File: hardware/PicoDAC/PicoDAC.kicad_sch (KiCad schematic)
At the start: 0 parts

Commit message: added level shifters, finished DAC schematics
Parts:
- added C1, C15, C16, C2, C3: 0.1uF, symbol Device:C_Small
- added C10, C11, C12, C13, C14, C5, C6, C9: 2.2uF, symbol Device:C_Small
- added C4: 4.7uF, symbol Device:C_Small
- added C7, C8: 15uF, symbol Device:C_Small
- added CN1: PJ-327A 5JJ, easyeda2kicad:AUDIO-SMD_PJ-327A5JJ, symbol easyeda2kicad:PJ-327A5JJ
- added R1, R2, R3: 10k, symbol Device:R_Small
- added R4: 200k, symbol Device:R_Small
- added R5, R6, R7, R8: 4.7k, symbol Device:R_Small
- added U1: CS43131-CNZR, easyeda2kicad:TQFN-40_L5.0-W5.0-P0.40-TL-EP3.5, symbol easyeda2kicad:CS43131-CNZR
- added U2: XIAO-RP2350-DIP, Seeed Studio XIAO Series Library:XIAO-RP2350-DIP, symbol Seeed_Studio_XIAO_Series:XIAO-RP2350-DIP
- added U3: PCA9306DCUR, easyeda2kicad:SSOP-8_L2.0-W2.3-P0.50-LS3.1-BR, symbol easyeda2kicad:PCA9306DCUR
- added U4: SN74AXC4T245PWR, easyeda2kicad:TSSOP-16_L5.0-W4.4-P0.65-LS6.4-BL, symbol easyeda2kicad:SN74AXC4T245PWR
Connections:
- new net: R6.2, U3.6 (SCL2)
- new net: R5.1, U3.5 (SDA2)
- new net: R4.2, U3.7 (VREF2), U3.8 (EN)
- new net: C8.2, C9.2, U1.9 (-VA)
- new net: C11.1, U1.21 (VCP_FILT+)
- new net: C14.1, U1.11 (FLYN_VA)
- new net: C14.2, U1.10 (FLYP_VA)
- new net: C12.2, U1.18 (VCP_FILT–)
- new net: C13.2, U1.20 (FLYN_VCP)
- new net: C13.1, C5.1, U1.23 (FLYC_VCP)
- new net: C5.2, U1.24 (FLYP_VCP)
- new net +1V8: C1.1, C10.1, C15.2, C2.2, C6.1, C7.1, R1.2, R7.1, R8.2, U1.25 (VCP), U1.31 (VL), U1.4 (VD), U1.7 (VA), U3.2 (VREF1), U4.16 (VCCB)
- new net +3.3V: C16.2, C3.1, C4.2, R2.1, R3.2, R4.1, R5.2, R6.1, U1.26 (VP), U4.1 (VCCA), U4.2 (1DIR), U4.3 (2DIR)
- new net DAC_FILT+: C7.2, U1.5 (FILT+)
- new net DAC_FILT-: C8.1, U1.6 (FILT–)
- new net DAC_HPOUTA: CN1.3, U1.14 (HPOUTA)
- new net DAC_HPOUTB: CN1.4, U1.16 (HPOUTB)
- new net DAC_HPREF_A: CN1.1, U1.13 (HPREFA)
- new net DAC_HPREF_B: CN1.2, U1.17 (HPREFB)
- new net DAC_HP_DETECT: CN1.5, U1.22 (HP_DETECT)
- new net DAC_I2C_SCL: R8.1, U1.1 (SCL), U3.3 (SCL1)
- new net DAC_I2C_SDA: R7.2, U1.39 (SDA), U3.4 (SDA1)
- new net DAC_I2S_LRCK1: U1.38 (LRCK1), U4.12 (1B2)
- new net DAC_I2S_SCLK1: U1.34 (SCLK1), U4.11 (2B1)
- new net DAC_I2S_SDIN1: U1.2 (SDIN1), U4.13 (1B1)
- new net DAC_MCLK: U1.37 (XTI/MCLK), U4.10 (2B2)
- new net DAC_RESET: R1.1, U1.28 (~{RESET})
- new net GND: C1.2, C10.2, C11.2, C12.1, C15.1, C16.1, C2.1, C3.2, C4.1, C6.2, C9.1, U1.19 (GNDCP), U1.30 (ADR), U1.35 (GNDD), U1.41 (EP), U1.8 (GNDA), U2.13 (GND), U3.1 (GND), U4.8 (GND), U4.9 (GND)
- new net LS1_1OE: R2.2, R3.1, U4.14 (~{2OE}), U4.15 (~{1OE})
- new net MCU_GP_00: U2.7 (GPIO0/D6/TX0)
- new net MCU_GP_01: U2.8 (GPIO1/D7/RX0)
- new net MCU_GP_02: U2.9 (GPIO2/D8/SPI0_SCK)
- new net MCU_GP_03: U2.11 (GPIO3/D10/SPI0_MOSI)
- new net MCU_GP_04: U2.10 (GPIO4/D9/SPI_MISO)
- new net MCU_GP_05: U2.4 (GPIO5/D3/SPI_CS)
- new net MCU_GP_06: U2.5 (GPIO6/D4/SDA1)
- new net MCU_GP_07: U2.6 (GPIO7/D5/SCL1)
- new net MCU_GP_26: U2.1 (GPIO26/D0/ADC0)
- new net MCU_GP_27: U2.2 (GPIO27/D1/ADC1)
- new net MCU_GP_28: U2.3 (GPIO28/D2/ADC2)
- new net VBUS: U2.14 (VBUS)
- no-connect marks 0 -> 9
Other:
- note added: "Always enabled"
- note added: "DAC"
- note added: "EXT_VCPFILT = 0"
- note added: "I2C LEVEL SHIFTER"
- note added: "I2S LEVEL SHIFTER"
- note added: "MCU"
- note added: "Will be pulled to GND on power up"
- note added: "Will be pulled to GND on power up, after MCU_LS_OE"

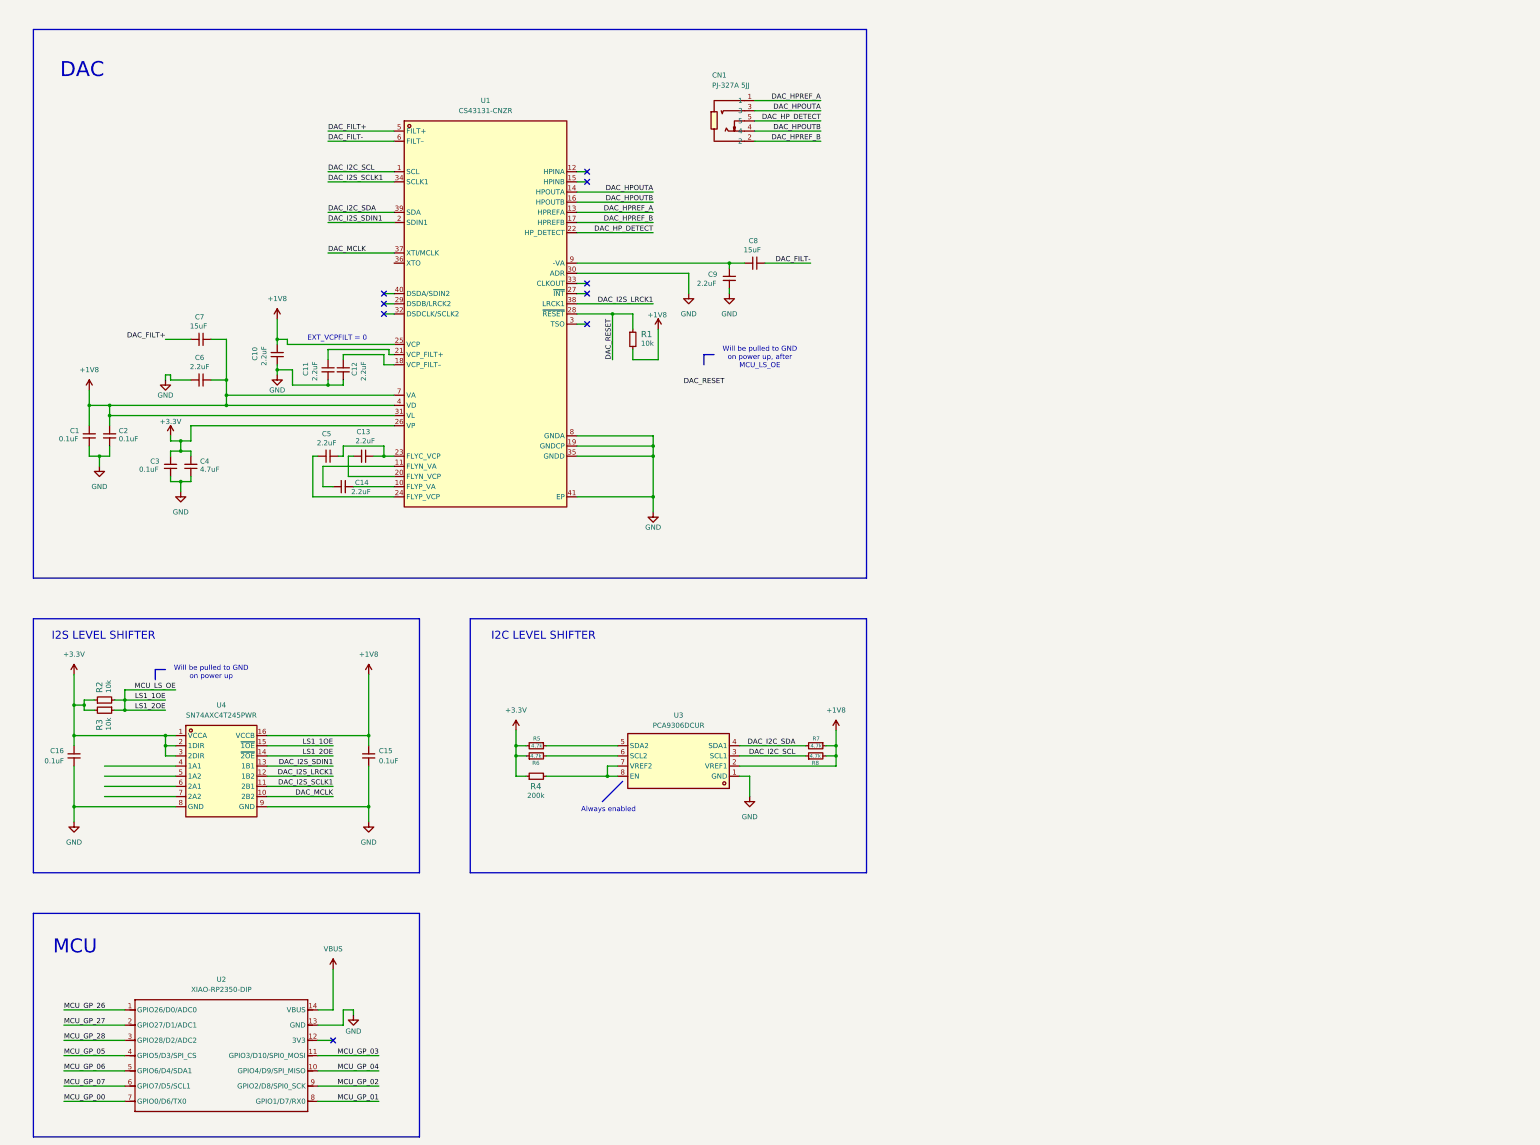
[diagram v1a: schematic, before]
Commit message: finished schematics (led, usb_c_m-m board + 1.8v voltage regulator)
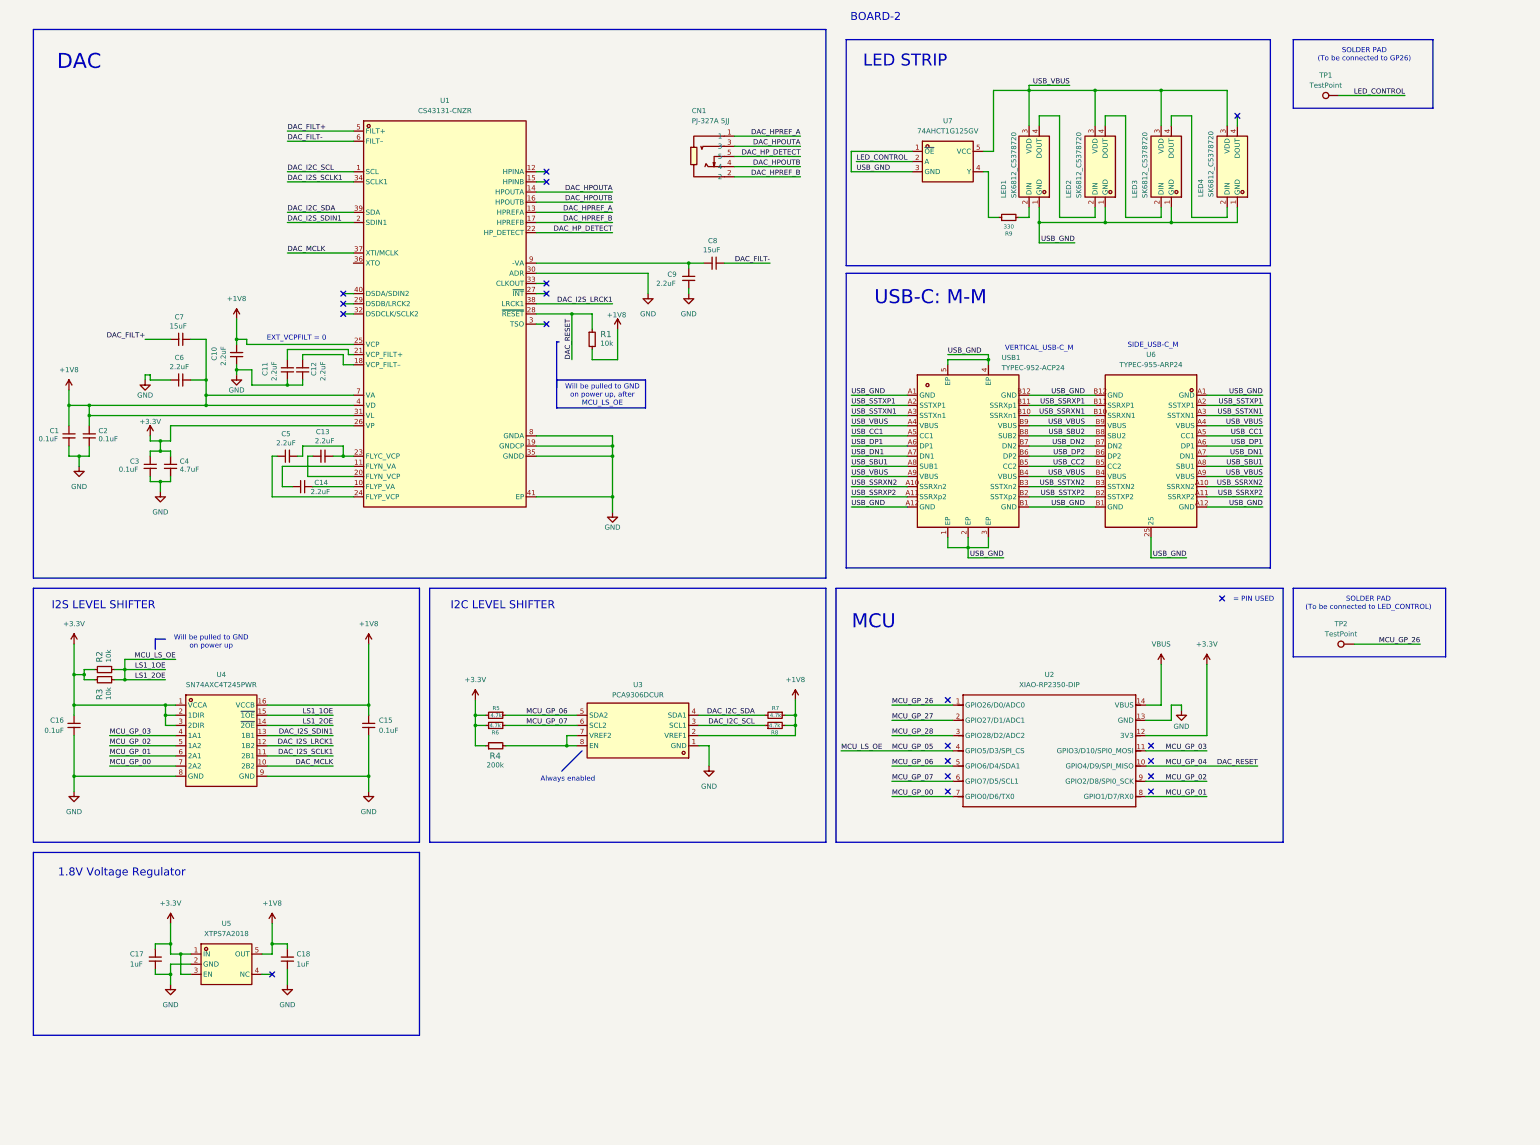
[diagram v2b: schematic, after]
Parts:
- added C17, C18: 1uF, symbol Device:C_Small
- added LED1, LED2, LED3, LED4: SK6812_C5378720, easyeda2kicad:LED-SMD_4P-L5.4-W5.0_SK6812, symbol easyeda2kicad:SK6812_C5378720
- added R9: 330, symbol Device:R_Small
- added TP1, TP2: TestPoint, TestPoint:TestPoint_Pad_D2.0mm, symbol Connector:TestPoint
- added U5: XTPS7A2018, easyeda2kicad:SOT-23-5_L3.0-W1.7-P0.95-LS2.8-BL, symbol easyeda2kicad:XTPS7A2018
- added U6: TYPEC-955-ARP24, easyeda2kicad:TYPE-C-SMD_TYPEC-955-ARP24, symbol easyeda2kicad:TYPEC-955-ARP24
- added U7: 74AHCT1G125GV, easyeda2kicad:SOT-23-5_L3.0-W1.7-P0.95-LS2.8-BL, symbol easyeda2kicad:74AHCT1G125GV
- added USB1: TYPEC-952-ACP24, easyeda2kicad:USB-C-SMD_TYPEC-952-ACP24, symbol easyeda2kicad:TYPEC-952-ACP24
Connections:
- net MCU_GP_04 is gone; now on net DAC_RESET: U2.10 (GPIO4/D9/SPI_MISO)
- net MCU_GP_05 is gone; now on net LS1_1OE: U2.4 (GPIO5/D3/SPI_CS)
- net +1V8: now also C18.2, U5.5 (OUT)
- net +3.3V: now also U2.12 (3V3), C17.1, U5.1 (IN), U5.3 (EN)
- net GND: now also C17.2, C18.1, U5.2 (GND)
- net MCU_GP_00: now also U4.7 (2A2)
- net MCU_GP_01: now also U4.6 (2A1)
- net MCU_GP_02: now also U4.5 (1A2)
- net MCU_GP_03: now also U4.4 (1A1)
- net MCU_GP_06: now also R5.1, U3.5 (SDA2)
- net MCU_GP_07: now also R6.2, U3.6 (SCL2)
- net MCU_GP_26: now also TP2.1
- new net: LED1.2 (DIN), R9.2
- new net: LED1.4 (DOUT), LED2.2 (DIN)
- new net: R9.1, U7.4 (Y)
- new net: LED2.4 (DOUT), LED3.2 (DIN)
- new net: LED3.4 (DOUT), LED4.2 (DIN)
- new net LED_CONTROL: TP1.1, U7.2 (A)
- new net USB_CC1: U6.A5 (CC1), USB1.A5 (CC1)
- new net USB_CC2: U6.B5 (CC2), USB1.B5 (CC2)
- new net USB_DN1: U6.A7 (DN1), USB1.A7 (DN1)
- new net USB_DN2: U6.B7 (DN2), USB1.B7 (DN2)
- new net USB_DP1: U6.A6 (DP1), USB1.A6 (DP1)
- new net USB_DP2: U6.B6 (DP2), USB1.B6 (DP2)
- new net USB_GND: LED1.1 (GND), LED2.1 (GND), LED3.1 (GND), LED4.1 (GND), U6.25, U6.A1 (GND), U6.A12 (GND), U6.B1 (GND), U6.B12 (GND), U7.1 (~{OE}), U7.3 (GND), USB1.1 (EP), USB1.2 (EP), USB1.3 (EP), USB1.4 (EP), USB1.5 (EP), USB1.A1 (GND), USB1.A12 (GND), USB1.B1 (GND), USB1.B12 (GND)
- new net USB_SBU1: U6.A8 (SBU1), USB1.A8 (SUB1)
- new net USB_SBU2: U6.B8 (SBU2), USB1.B8 (SUB2)
- new net USB_SSRXN1: U6.B10 (SSRXN1), USB1.B10 (SSRXn1)
- new net USB_SSRXN2: U6.A10 (SSRXN2), USB1.A10 (SSRXn2)
- new net USB_SSRXP1: U6.B11 (SSRXP1), USB1.B11 (SSRXp1)
- new net USB_SSRXP2: U6.A11 (SSRXP2), USB1.A11 (SSRXp2)
- new net USB_SSTXN1: U6.A3 (SSTXN1), USB1.A3 (SSTXn1)
- new net USB_SSTXN2: U6.B3 (SSTXN2), USB1.B3 (SSTXn2)
- new net USB_SSTXP1: U6.A2 (SSTXP1), USB1.A2 (SSTXP1)
- new net USB_SSTXP2: U6.B2 (SSTXP2), USB1.B2 (SSTXp2)
- new net USB_VBUS: LED1.3 (VDD), LED2.3 (VDD), LED3.3 (VDD), LED4.3 (VDD), U6.A4 (VBUS), U6.A9 (VBUS), U6.B4 (VBUS), U6.B9 (VBUS), U7.5 (VCC), USB1.A4 (VBUS), USB1.A9 (VBUS), USB1.B4 (VBUS), USB1.B9 (VBUS)
- no-connect marks 9 -> 20
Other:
- note added: "1.8V Voltage Regulator"
- note added: "= PIN USED"
- note added: "BOARD-2"
- note added: "LED STRIP"
- note added: "SIDE_USB-C_M"
- note added: "SOLDER PAD (To be connected to GP26)"
- note added: "SOLDER PAD (To be connected to LED_CONTROL)"
- note added: "USB-C: M-M"
- note added: "VERTICAL_USB-C_M"
- moved on the sheet: C1, C10, C11, C12, C13, C14, C15, C16, C2, C3, C4, C5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

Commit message: updated footprints for resistors, capacitors
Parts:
- C1, C15, C16, C2, C3: footprint (none) -> easyeda2kicad:C0402; LCSC Part (none) -> C60474; MPN (none) -> CC0402KRX7R7BB104
- C10, C11, C12, C13, C14, C5, C6, C9: footprint (none) -> easyeda2kicad:C0201; LCSC Part (none) -> C335106; MPN (none) -> GRM033R61A225KE47D
- C17, C18: footprint (none) -> easyeda2kicad:C0402; LCSC Part (none) -> C52923; MPN (none) -> CL05A105KA5NQNC
- C4: footprint (none) -> easyeda2kicad:C0603; LCSC Part (none) -> C19666; MPN (none) -> CL10A475KO8NNNC
- C7, C8: footprint (none) -> easyeda2kicad:C1210; LCSC Part (none) -> C694469; MPN (none) -> C3225X7R1C156MT000N
- R1, R2, R3: footprint (none) -> easyeda2kicad:R0402; LCSC Part (none) -> C60490; MPN (none) -> RC0402FR-0710KL
- R4: footprint (none) -> easyeda2kicad:R0402; LCSC Part (none) -> C25764; MPN (none) -> 0402WGF2003TCE
- R5, R6, R7, R8: footprint (none) -> easyeda2kicad:R0402; LCSC Part (none) -> C105871; MPN (none) -> RC0402FR-074K7L
- R9: footprint (none) -> easyeda2kicad:R0402; LCSC Part (none) -> C105875; MPN (none) -> RC0402FR-07330RL
- TP1, TP2, U2: now left out of the parts list

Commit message: main board rev1
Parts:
- U6: footprint easyeda2kicad:TYPE-C-SMD_TYPEC-955-ARP24 -> easyeda2kicad:USB-C-SMD_TYPE-C-24P-GTJB-040; symbol easyeda2kicad:TYPEC-955-ARP24 -> easyeda2kicad:TYPE-C24P-GTJB040; LCSC Part C2895018 -> C3151751; MPN TYPEC-955-ARP24 -> TYPE-C 24P-GTJB 040; Manufacturer XUNPU(讯普) -> SHOU HAN(首韩)
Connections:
- net USB_GND: now also U6.26 (GND)
- net USB_SBU1: no longer names the net of U6.A8 (SBU1)
- net USB_SBU1: no longer USB1.A8 (SUB1)
- net USB_SBU2: no longer names the net of U6.B8 (SBU2)
- net USB_SBU2: no longer USB1.B8 (SUB2)
- net USB_SSRXN1: no longer names the net of U6.B10 (SSRXn1)
- net USB_SSRXN1: no longer USB1.B10 (SSRXn1)
- net USB_SSRXN2: no longer names the net of U6.A10 (SSRXn2)
- net USB_SSRXN2: no longer USB1.A10 (SSRXn2)
- net USB_SSRXP1: no longer names the net of U6.B11 (SSRXp1)
- net USB_SSRXP1: no longer USB1.B11 (SSRXp1)
- net USB_SSRXP2: no longer names the net of U6.A11 (SSRXp2)
- net USB_SSRXP2: no longer USB1.A11 (SSRXp2)
- net USB_SSTXN1: no longer names the net of U6.A3 (SSTXn1)
- net USB_SSTXN1: no longer USB1.A3 (SSTXn1)
- net USB_SSTXN2: no longer names the net of U6.B3 (SSTXn2)
- net USB_SSTXN2: no longer USB1.B3 (SSTXn2)
- net USB_SSTXP1: no longer names the net of U6.A2 (SSTXP1)
- net USB_SSTXP1: no longer USB1.A2 (SSTXP1)
- net USB_SSTXP2: no longer names the net of U6.B2 (SSTXp2)
- net USB_SSTXP2: no longer USB1.B2 (SSTXp2)
- no-connect marks 20 -> 39
